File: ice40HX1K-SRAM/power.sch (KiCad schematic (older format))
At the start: 20 parts

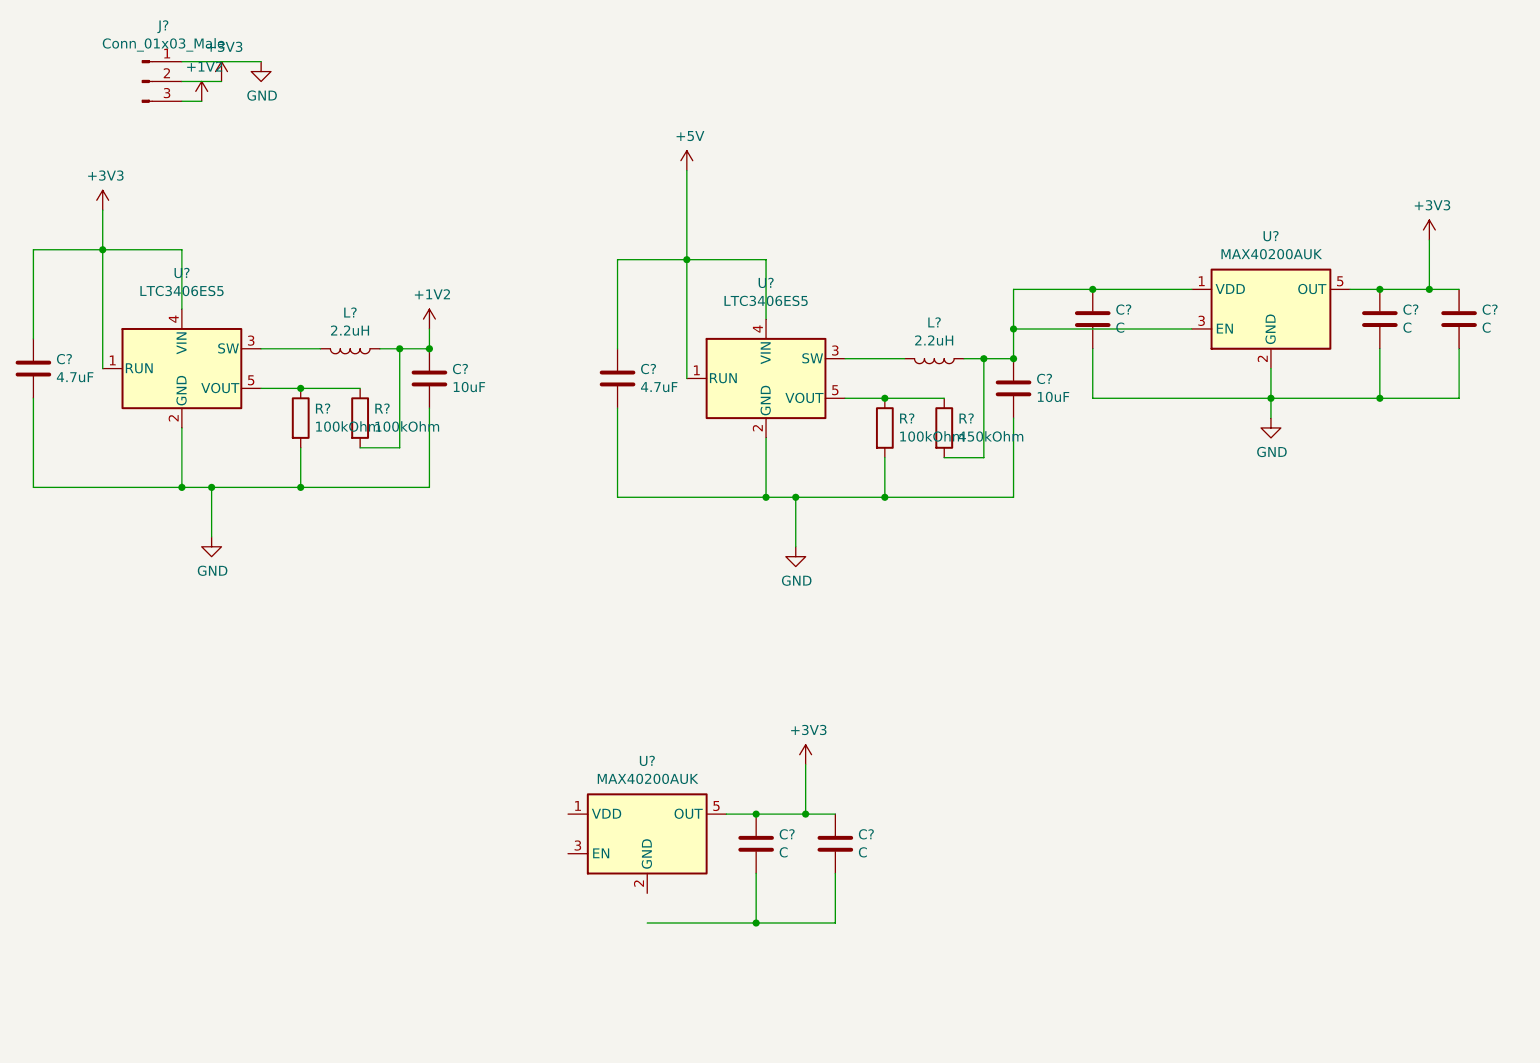
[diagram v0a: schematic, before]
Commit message: wiring FPGA nRF52 and ATSAMD11
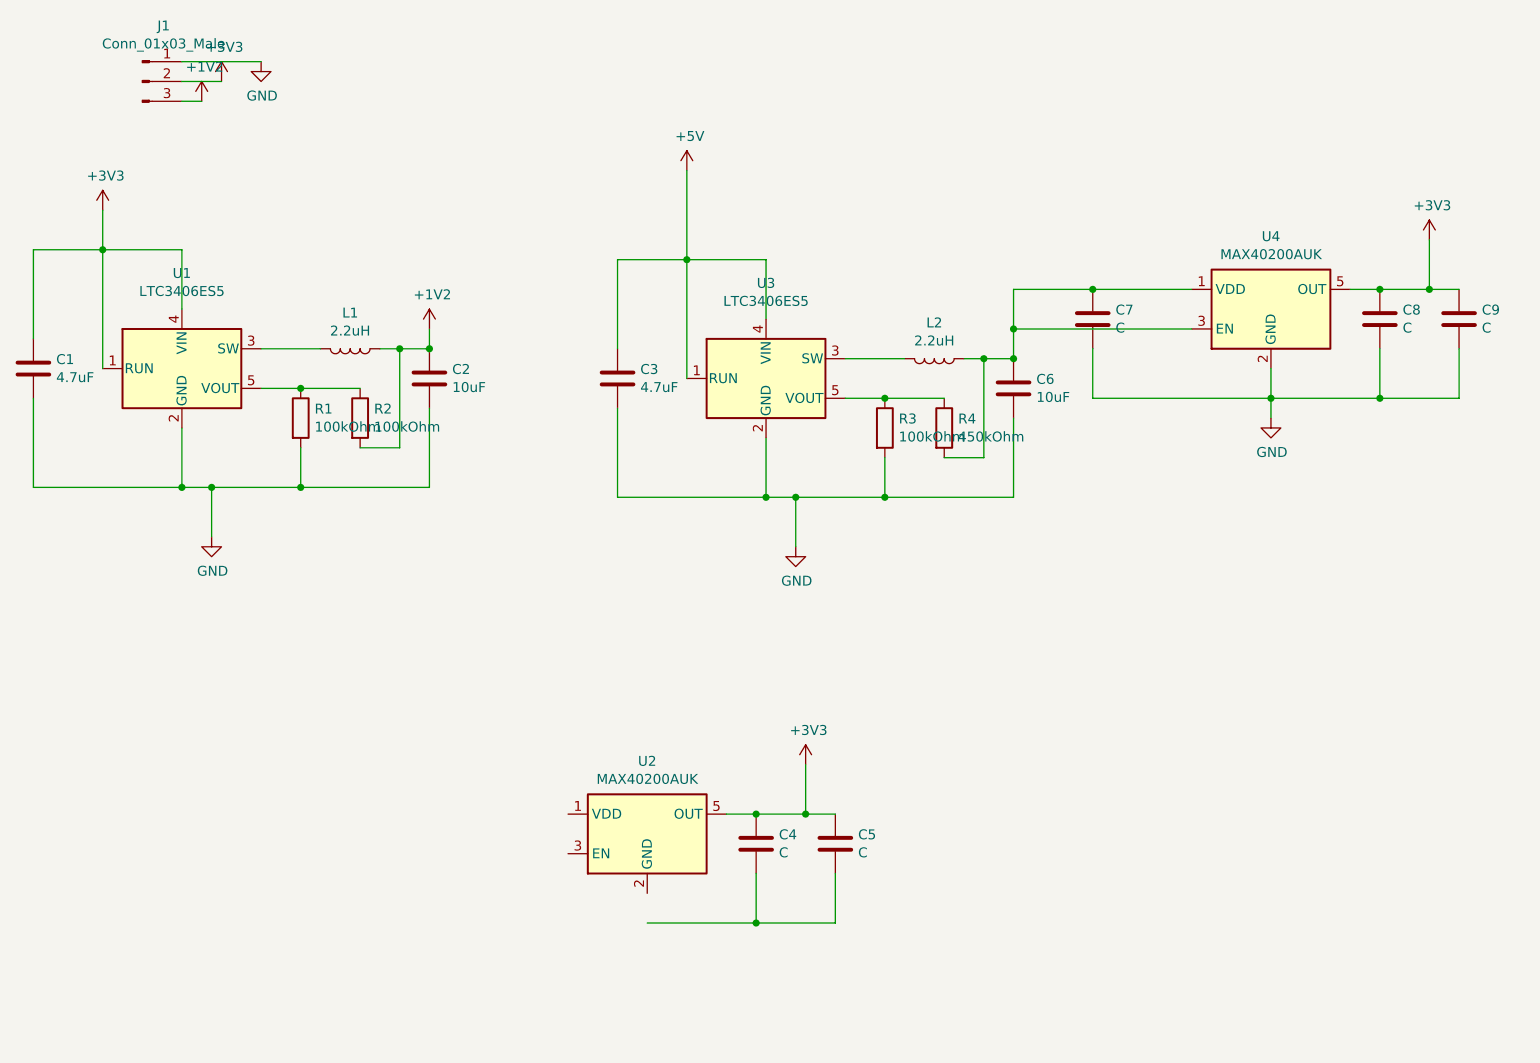
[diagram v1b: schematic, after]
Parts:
- gave numbers to parts that had none: 20
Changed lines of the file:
@@
 $EndDescr
 $Comp
-L Regulator_Switching:LTC3406ES5 U?
+L Regulator_Switching:LTC3406ES5 U1
 U 1 1 5E5E25FE
 P 1850 2500
-F 0 "U?" H 1850 2981 50  0000 C CNN
+F 0 "U1" H 1850 2981 50  0000 C CNN
 F 1 "LTC3406ES5" H 1850 2890 50  0000 C CNN
 F 2 "Package_TO_SOT_SMD:TSOT-23-5" H 2550 2250 50  0001 C CNN
@@
 $EndComp
 $Comp
-L Device:L L?
+L Device:L L1
 U 1 1 5E5E2604
 P 2700 2400
-F 0 "L?" V 2519 2400 50  0000 C CNN
+F 0 "L1" V 2519 2400 50  0000 C CNN
 F 1 "2.2uH" V 2610 2400 50  0000 C CNN
 F 2 "Inductor_SMD:L_1210_3225Metric" H 2700 2400 50  0001 C CNN
@@
 $EndComp
 $Comp
-L Device:C C?
+L Device:C C2
 U 1 1 5E5E260A
 P 3100 2550
-F 0 "C?" H 3215 2596 50  0000 L CNN
+F 0 "C2" H 3215 2596 50  0000 L CNN
 F 1 "10uF" H 3215 2505 50  0000 L CNN
 F 2 "Capacitor_SMD:C_1206_3216Metric" H 3138 2400 50  0001 C CNN
@@
 $EndComp
 $Comp
-L Device:C C?
+L Device:C C1
 U 1 1 5E5E2610
 P 1100 2500
-F 0 "C?" H 1215 2546 50  0000 L CNN
+F 0 "C1" H 1215 2546 50  0000 L CNN
 F 1 "4.7uF" H 1215 2455 50  0000 L CNN
 F 2 "Capacitor_SMD:C_1206_3216Metric" H 1138 2350 50  0001 C CNN
@@
 $EndComp
 $Comp
-L Device:R R?
+L Device:R R1
 U 1 1 5E5E2616
 P 2450 2750
-F 0 "R?" H 2520 2796 50  0000 L CNN
+F 0 "R1" H 2520 2796 50  0000 L CNN
 F 1 "100kOhm" H 2520 2705 50  0000 L CNN
 F 2 "Resistor_SMD:R_1206_3216Metric" V 2380 2750 50  0001 C CNN
@@
 $EndComp
 $Comp
-L Device:R R?
+L Device:R R2
 U 1 1 5E5E261C
 P 2750 2750
-F 0 "R?" H 2820 2796 50  0000 L CNN
+F 0 "R2" H 2820 2796 50  0000 L CNN
 F 1 "100kOhm" H 2820 2705 50  0000 L CNN
 F 2 "Resistor_SMD:R_1206_3216Metric" V 2680 2750 50  0001 C CNN
@@
 Connection ~ 2450 3100
 $Comp
-L power:+1V2 #PWR?
+L power:+1V2 #PWR06
 U 1 1 5E5E263A
 P 3100 2300
-F 0 "#PWR?" H 3100 2150 50  0001 C CNN
+F 0 "#PWR06" H 3100 2150 50  0001 C CNN
 F 1 "+1V2" H 3115 2473 50  0000 C CNN
 F 2 "" H 3100 2300 50  0001 C CNN
@@
 Connection ~ 3100 2400
 $Comp
-L power:GND #PWR?
+L power:GND #PWR03
 U 1 1 5E5E2642
 P 2000 3350
-F 0 "#PWR?" H 2000 3100 50  0001 C CNN
+F 0 "#PWR03" H 2000 3100 50  0001 C CNN
 F 1 "GND" H 2005 3177 50  0000 C CNN
 F 2 "" H 2000 3350 50  0001 C CNN
@@
 	2000 3100 2450 3100
 $Comp
-L power:+3V3 #PWR?
+L power:+3V3 #PWR01
 U 1 1 5E5E264B
 P 1450 1700
-F 0 "#PWR?" H 1450 1550 50  0001 C CNN
+F 0 "#PWR01" H 1450 1550 50  0001 C CNN
 F 1 "+3V3" H 1465 1873 50  0000 C CNN
 F 2 "" H 1450 1700 50  0001 C CNN
@@
 	1450 1700 1450 1900
 $Comp
-L Connector:Conn_01x03_Male J?
+L Connector:Conn_01x03_Male J1
 U 1 1 5E5E2652
 P 1650 1050
-F 0 "J?" H 1758 1331 50  0000 C CNN
+F 0 "J1" H 1758 1331 50  0000 C CNN
 F 1 "Conn_01x03_Male" H 1758 1240 50  0000 C CNN
 F 2 "Connector_PinHeader_2.54mm:PinHeader_1x03_P2.54mm_Vertical" H 1650 1050 50  0001 C CNN
@@
 $EndComp
 $Comp
-L power:GND #PWR?
+L power:GND #PWR05
 U 1 1 5E5E2658
 P 2250 950
-F 0 "#PWR?" H 2250 700 50  0001 C CNN
+F 0 "#PWR05" H 2250 700 50  0001 C CNN
 F 1 "GND" H 2255 777 50  0000 C CNN
 F 2 "" H 2250 950 50  0001 C CNN
@@
 $EndComp
 $Comp
-L power:+3V3 #PWR?
+L power:+3V3 #PWR04
 U 1 1 5E5E265E
 P 2050 1050
-F 0 "#PWR?" H 2050 900 50  0001 C CNN
+F 0 "#PWR04" H 2050 900 50  0001 C CNN
 F 1 "+3V3" H 2065 1223 50  0000 C CNN
 F 2 "" H 2050 1050 50  0001 C CNN
@@
 $EndComp
 $Comp
-L power:+1V2 #PWR?
+L power:+1V2 #PWR02
 U 1 1 5E5E2664
 P 1950 1150
-F 0 "#PWR?" H 1950 1000 50  0001 C CNN
+F 0 "#PWR02" H 1950 1000 50  0001 C CNN
 F 1 "+1V2" H 1965 1323 50  0000 C CNN
 F 2 "" H 1950 1150 50  0001 C CNN
@@
 	1850 950  2250 950
 $Comp
-L Regulator_Switching:LTC3406ES5 U?
+L Regulator_Switching:LTC3406ES5 U3
 U 1 1 5E5F3EED
 P 4800 2550
-F 0 "U?" H 4800 3031 50  0000 C CNN
+F 0 "U3" H 4800 3031 50  0000 C CNN
 F 1 "LTC3406ES5" H 4800 2940 50  0000 C CNN
 F 2 "Package_TO_SOT_SMD:TSOT-23-5" H 5500 2300 50  0001 C CNN
@@
 $EndComp
 $Comp
-L Device:L L?
+L Device:L L2
 U 1 1 5E5F3EF3
 P 5650 2450
-F 0 "L?" V 5469 2450 50  0000 C CNN
+F 0 "L2" V 5469 2450 50  0000 C CNN
 F 1 "2.2uH" V 5560 2450 50  0000 C CNN
 F 2 "Inductor_SMD:L_1210_3225Metric" H 5650 2450 50  0001 C CNN
@@
 $EndComp
 $Comp
-L Device:C C?
+L Device:C C6
 U 1 1 5E5F3EF9
 P 6050 2600
-F 0 "C?" H 6165 2646 50  0000 L CNN
+F 0 "C6" H 6165 2646 50  0000 L CNN
 F 1 "10uF" H 6165 2555 50  0000 L CNN
 F 2 "Capacitor_SMD:C_1206_3216Metric" H 6088 2450 50  0001 C CNN
@@
 $EndComp
 $Comp
-L Device:C C?
+L Device:C C3
 U 1 1 5E5F3EFF
 P 4050 2550
-F 0 "C?" H 4165 2596 50  0000 L CNN
+F 0 "C3" H 4165 2596 50  0000 L CNN
 F 1 "4.7uF" H 4165 2505 50  0000 L CNN
 F 2 "Capacitor_SMD:C_1206_3216Metric" H 4088 2400 50  0001 C CNN
@@
 $EndComp
 $Comp
-L Device:R R?
+L Device:R R3
 U 1 1 5E5F3F05
 P 5400 2800
-F 0 "R?" H 5470 2846 50  0000 L CNN
+F 0 "R3" H 5470 2846 50  0000 L CNN
 F 1 "100kOhm" H 5470 2755 50  0000 L CNN
 F 2 "Resistor_SMD:R_1206_3216Metric" V 5330 2800 50  0001 C CNN
@@
 $EndComp
 $Comp
-L Device:R R?
+L Device:R R4
 U 1 1 5E5F3F0B
 P 5700 2800
-F 0 "R?" H 5770 2846 50  0000 L CNN
+F 0 "R4" H 5770 2846 50  0000 L CNN
 F 1 "450kOhm" H 5770 2755 50  0000 L CNN
 F 2 "Resistor_SMD:R_0402_1005Metric" V 5630 2800 50  0001 C CNN
@@
 Connection ~ 5400 3150
 $Comp
-L power:GND #PWR?
+L power:GND #PWR08
 U 1 1 5E5F3F31
 P 4950 3400
-F 0 "#PWR?" H 4950 3150 50  0001 C CNN
+F 0 "#PWR08" H 4950 3150 50  0001 C CNN
 F 1 "GND" H 4955 3227 50  0000 C CNN
 F 2 "" H 4950 3400 50  0001 C CNN
@@
 	4950 3150 5400 3150
 $Comp
-L power:+5V #PWR?
+L power:+5V #PWR07
 U 1 1 5E5F763C
 P 4400 1500
-F 0 "#PWR?" H 4400 1350 50  0001 C CNN
+F 0 "#PWR07" H 4400 1350 50  0001 C CNN
 F 1 "+5V" H 4415 1673 50  0000 C CNN
 F 2 "" H 4400 1500 50  0001 C CNN
@@
 	4400 1500 4400 1950
 $Comp
-L Analog_Switch:MAX40200AUK U?
+L Analog_Switch:MAX40200AUK U2
 U 1 1 5E608631
 P 4200 4850
-F 0 "U?" H 4200 5217 50  0000 C CNN
+F 0 "U2" H 4200 5217 50  0000 C CNN
 F 1 "MAX40200AUK" H 4200 5126 50  0000 C CNN
 F 2 "Package_TO_SOT_SMD:SOT-23-5" H 4200 5350 50  0001 C CNN
@@
 $EndComp
 $Comp
-L Analog_Switch:MAX40200AUK U?
+L Analog_Switch:MAX40200AUK U4
 U 1 1 5E608F29
 P 7350 2200
-F 0 "U?" H 7350 2567 50  0000 C CNN
+F 0 "U4" H 7350 2567 50  0000 C CNN
 F 1 "MAX40200AUK" H 7350 2476 50  0000 C CNN
 F 2 "Package_TO_SOT_SMD:SOT-23-5" H 7350 2700 50  0001 C CNN
@@
 $EndComp
 $Comp
-L power:+3V3 #PWR?
+L power:+3V3 #PWR011
 U 1 1 5E60C10F
 P 8150 1850
-F 0 "#PWR?" H 8150 1700 50  0001 C CNN
+F 0 "#PWR011" H 8150 1700 50  0001 C CNN
 F 1 "+3V3" H 8165 2023 50  0000 C CNN
 F 2 "" H 8150 1850 50  0001 C CNN
@@
 	6050 2300 6050 2100
 $Comp
-L Device:C C?
+L Device:C C7
 U 1 1 5E60FC3E
 P 6450 2250
-F 0 "C?" H 6565 2296 50  0000 L CNN
+F 0 "C7" H 6565 2296 50  0000 L CNN
 F 1 "C" H 6565 2205 50  0000 L CNN
 F 2 "" H 6488 2100 50  0001 C CNN
@@
 	6450 2100 6950 2100
 $Comp
-L Device:C C?
+L Device:C C8
 U 1 1 5E61086D
 P 7900 2250
-F 0 "C?" H 8015 2296 50  0000 L CNN
+F 0 "C8" H 8015 2296 50  0000 L CNN
 F 1 "C" H 8015 2205 50  0000 L CNN
 F 2 "" H 7938 2100 50  0001 C CNN
@@
 $EndComp
 $Comp
-L Device:C C?
+L Device:C C9
 U 1 1 5E610C79
 P 8300 2250
-F 0 "C?" H 8415 2296 50  0000 L CNN
+F 0 "C9" H 8415 2296 50  0000 L CNN
 F 1 "C" H 8415 2205 50  0000 L CNN
 F 2 "" H 8338 2100 50  0001 C CNN
@@
 	8150 2100 8300 2100
 $Comp
-L power:GND #PWR?
+L power:GND #PWR010
 U 1 1 5E6126DE
 P 7350 2750
-F 0 "#PWR?" H 7350 2500 50  0001 C CNN
+F 0 "#PWR010" H 7350 2500 50  0001 C CNN
 F 1 "GND" H 7355 2577 50  0000 C CNN
 F 2 "" H 7350 2750 50  0001 C CNN
@@
 	7900 2650 7350 2650
 $Comp
-L power:+3V3 #PWR?
+L power:+3V3 #PWR09
 U 1 1 5E61F7B9
 P 5000 4500
-F 0 "#PWR?" H 5000 4350 50  0001 C CNN
+F 0 "#PWR09" H 5000 4350 50  0001 C CNN
 F 1 "+3V3" H 5015 4673 50  0000 C CNN
 F 2 "" H 5000 4500 50  0001 C CNN
@@
 	5000 4500 5000 4750
 $Comp
-L Device:C C?
+L Device:C C4
 U 1 1 5E61F7C0
 P 4750 4900
-F 0 "C?" H 4865 4946 50  0000 L CNN
+F 0 "C4" H 4865 4946 50  0000 L CNN
 F 1 "C" H 4865 4855 50  0000 L CNN
 F 2 "" H 4788 4750 50  0001 C CNN
@@
 $EndComp
 $Comp
-L Device:C C?
+L Device:C C5
 U 1 1 5E61F7C6
 P 5150 4900
-F 0 "C?" H 5265 4946 50  0000 L CNN
+F 0 "C5" H 5265 4946 50  0000 L CNN
 F 1 "C" H 5265 4855 50  0000 L CNN
 F 2 "" H 5188 4750 50  0001 C CNN

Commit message: wiring FPGA
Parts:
- added BT1: Battery_Cell, symbol Device:Battery_Cell
- added C?: C, symbol Device:C
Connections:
- net at U2.1 (VDD): now also U2.3 (EN), BT1.1 (+), C?.1
- net at U2.2 (GND): now also C4.2, C5.2, BT1.2 (-), C?.2
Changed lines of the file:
@@
 	4750 5050 4750 5300
 Connection ~ 4750 5300
+$Comp
+L Device:Battery_Cell BT1
+U 1 1 5E6EFF2C
+P 2950 4950
+F 0 "BT1" H 3068 5046 50  0000 L CNN
+F 1 "Battery_Cell" H 3068 4955 50  0000 L CNN
+F 2 "" V 2950 5010 50  0001 C CNN
+F 3 "~" V 2950 5010 50  0001 C CNN
+	1    2950 4950
+	1    0    0    -1
+$EndComp
 Wire Wire Line
-	4750 5300 4200 5300
+	2950 4750 3400 4750
+Wire Wire Line
+	3600 4750 3600 4950
+Wire Wire Line
+	3600 4950 3800 4950
+Connection ~ 3600 4750
+Wire Wire Line
+	3600 4750 3800 4750
+Wire Wire Line
+	2950 5050 2950 5300
+Wire Wire Line
+	2950 5300 3400 5300
+Wire Wire Line
+	4200 5150 4200 5300
+Connection ~ 4200 5300
+Wire Wire Line
+	4200 5300 4750 5300
+$Comp
+L Device:C C?
+U 1 1 5E6F85E4
+P 3400 5000
+F 0 "C?" H 3515 5046 50  0000 L CNN
+F 1 "C" H 3515 4955 50  0000 L CNN
+F 2 "" H 3438 4850 50  0001 C CNN
+F 3 "~" H 3400 5000 50  0001 C CNN
+	1    3400 5000
+	1    0    0    -1
+$EndComp
+Wire Wire Line
+	3400 4850 3400 4750
+Connection ~ 3400 4750
+Wire Wire Line
+	3400 4750 3600 4750
+Wire Wire Line
+	3400 5150 3400 5300
+Connection ~ 3400 5300
+Wire Wire Line
+	3400 5300 4200 5300
 $EndSCHEMATC

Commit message: wiring FPGA
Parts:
- C4, C7, C8: value C -> 0.1uF
- C5, C9: value C -> 10uF
- C57: renamed from C?; value C -> 0.1uF
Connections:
- net GND: now also BT1.2 (-), C4.2, C5.2, C57.2, U2.2 (GND)
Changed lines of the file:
@@
 P 6450 2250
 F 0 "C7" H 6565 2296 50  0000 L CNN
-F 1 "C" H 6565 2205 50  0000 L CNN
+F 1 "0.1uF" H 6565 2205 50  0000 L CNN
 F 2 "" H 6488 2100 50  0001 C CNN
 F 3 "~" H 6450 2250 50  0001 C CNN
@@
 P 7900 2250
 F 0 "C8" H 8015 2296 50  0000 L CNN
-F 1 "C" H 8015 2205 50  0000 L CNN
+F 1 "0.1uF" H 8015 2205 50  0000 L CNN
 F 2 "" H 7938 2100 50  0001 C CNN
 F 3 "~" H 7900 2250 50  0001 C CNN
@@
 P 8300 2250
 F 0 "C9" H 8415 2296 50  0000 L CNN
-F 1 "C" H 8415 2205 50  0000 L CNN
+F 1 "10uF" H 8415 2205 50  0000 L CNN
 F 2 "" H 8338 2100 50  0001 C CNN
 F 3 "~" H 8300 2250 50  0001 C CNN
@@
 P 4750 4900
 F 0 "C4" H 4865 4946 50  0000 L CNN
-F 1 "C" H 4865 4855 50  0000 L CNN
+F 1 "0.1uF" H 4865 4855 50  0000 L CNN
 F 2 "" H 4788 4750 50  0001 C CNN
 F 3 "~" H 4750 4900 50  0001 C CNN
@@
 P 5150 4900
 F 0 "C5" H 5265 4946 50  0000 L CNN
-F 1 "C" H 5265 4855 50  0000 L CNN
+F 1 "10uF" H 5265 4855 50  0000 L CNN
 F 2 "" H 5188 4750 50  0001 C CNN
 F 3 "~" H 5150 4900 50  0001 C CNN
@@
 	4200 5300 4750 5300
 $Comp
-L Device:C C?
+L Device:C C57
 U 1 1 5E6F85E4
 P 3400 5000
-F 0 "C?" H 3515 5046 50  0000 L CNN
-F 1 "C" H 3515 4955 50  0000 L CNN
+F 0 "C57" H 3515 5046 50  0000 L CNN
+F 1 "0.1uF" H 3515 4955 50  0000 L CNN
 F 2 "" H 3438 4850 50  0001 C CNN
 F 3 "~" H 3400 5000 50  0001 C CNN
@@
 Wire Wire Line
 	3400 5300 4200 5300
+$Comp
+L power:GND #PWR0101
+U 1 1 5E7038EC
+P 4200 5700
+F 0 "#PWR0101" H 4200 5450 50  0001 C CNN
+F 1 "GND" H 4205 5527 50  0000 C CNN
+F 2 "" H 4200 5700 50  0001 C CNN
+F 3 "" H 4200 5700 50  0001 C CNN
+	1    4200 5700
+	1    0    0    -1
+$EndComp
+Wire Wire Line
+	4200 5300 4200 5700
+$Comp
+L power:PWR_FLAG #FLG0101
+U 1 1 5E70864B
+P 2950 4750
+F 0 "#FLG0101" H 2950 4825 50  0001 C CNN
+F 1 "PWR_FLAG" H 2950 4923 50  0000 C CNN
+F 2 "" H 2950 4750 50  0001 C CNN
+F 3 "~" H 2950 4750 50  0001 C CNN
+	1    2950 4750
+	1    0    0    -1
+$EndComp
+Connection ~ 2950 4750
+$Comp
+L power:PWR_FLAG #FLG0102
+U 1 1 5E70C20E
+P 6450 2100
+F 0 "#FLG0102" H 6450 2175 50  0001 C CNN
+F 1 "PWR_FLAG" H 6450 2273 50  0000 C CNN
+F 2 "" H 6450 2100 50  0001 C CNN
+F 3 "~" H 6450 2100 50  0001 C CNN
+	1    6450 2100
+	1    0    0    -1
+$EndComp
+$Comp
+L power:PWR_FLAG #FLG0103
+U 1 1 5E70E2F6
+P 4050 1950
+F 0 "#FLG0103" H 4050 2025 50  0001 C CNN
+F 1 "PWR_FLAG" H 4050 2123 50  0000 C CNN
+F 2 "" H 4050 1950 50  0001 C CNN
+F 3 "~" H 4050 1950 50  0001 C CNN
+	1    4050 1950
+	1    0    0    -1
+$EndComp
+Connection ~ 4050 1950
 $EndSCHEMATC

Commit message: wiring FPGA
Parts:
- C1, C3: footprint Capacitor_SMD:C_1206_3216Metric -> Capacitor_SMD:C_0402_1005Metric
- C2, C6: footprint Capacitor_SMD:C_1206_3216Metric -> Capacitor_SMD:C_0603_1608Metric
- C4, C7, C8: footprint (none) -> Capacitor_SMD:C_0402_1005Metric
- C5, C9: footprint (none) -> Capacitor_SMD:C_0603_1608Metric
- R1, R2, R3: footprint Resistor_SMD:R_1206_3216Metric -> Resistor_SMD:R_0402_1005Metric
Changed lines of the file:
@@
 F 0 "C2" H 3215 2596 50  0000 L CNN
 F 1 "10uF" H 3215 2505 50  0000 L CNN
-F 2 "Capacitor_SMD:C_1206_3216Metric" H 3138 2400 50  0001 C CNN
+F 2 "Capacitor_SMD:C_0603_1608Metric" H 3138 2400 50  0001 C CNN
 F 3 "~" H 3100 2550 50  0001 C CNN
 	1    3100 2550
@@
 F 0 "C1" H 1215 2546 50  0000 L CNN
 F 1 "4.7uF" H 1215 2455 50  0000 L CNN
-F 2 "Capacitor_SMD:C_1206_3216Metric" H 1138 2350 50  0001 C CNN
+F 2 "Capacitor_SMD:C_0402_1005Metric" H 1138 2350 50  0001 C CNN
 F 3 "~" H 1100 2500 50  0001 C CNN
 	1    1100 2500
@@
 F 0 "R1" H 2520 2796 50  0000 L CNN
 F 1 "100kOhm" H 2520 2705 50  0000 L CNN
-F 2 "Resistor_SMD:R_1206_3216Metric" V 2380 2750 50  0001 C CNN
+F 2 "Resistor_SMD:R_0402_1005Metric" V 2380 2750 50  0001 C CNN
 F 3 "~" H 2450 2750 50  0001 C CNN
 	1    2450 2750
@@
 F 0 "R2" H 2820 2796 50  0000 L CNN
 F 1 "100kOhm" H 2820 2705 50  0000 L CNN
-F 2 "Resistor_SMD:R_1206_3216Metric" V 2680 2750 50  0001 C CNN
+F 2 "Resistor_SMD:R_0402_1005Metric" V 2680 2750 50  0001 C CNN
 F 3 "~" H 2750 2750 50  0001 C CNN
 	1    2750 2750
@@
 F 0 "C6" H 6165 2646 50  0000 L CNN
 F 1 "10uF" H 6165 2555 50  0000 L CNN
-F 2 "Capacitor_SMD:C_1206_3216Metric" H 6088 2450 50  0001 C CNN
+F 2 "Capacitor_SMD:C_0603_1608Metric" H 6088 2450 50  0001 C CNN
 F 3 "~" H 6050 2600 50  0001 C CNN
 	1    6050 2600
@@
 F 0 "C3" H 4165 2596 50  0000 L CNN
 F 1 "4.7uF" H 4165 2505 50  0000 L CNN
-F 2 "Capacitor_SMD:C_1206_3216Metric" H 4088 2400 50  0001 C CNN
+F 2 "Capacitor_SMD:C_0402_1005Metric" H 4088 2400 50  0001 C CNN
 F 3 "~" H 4050 2550 50  0001 C CNN
 	1    4050 2550
@@
 F 0 "R3" H 5470 2846 50  0000 L CNN
 F 1 "100kOhm" H 5470 2755 50  0000 L CNN
-F 2 "Resistor_SMD:R_1206_3216Metric" V 5330 2800 50  0001 C CNN
+F 2 "Resistor_SMD:R_0402_1005Metric" V 5330 2800 50  0001 C CNN
 F 3 "~" H 5400 2800 50  0001 C CNN
 	1    5400 2800
@@
 F 0 "C7" H 6565 2296 50  0000 L CNN
 F 1 "0.1uF" H 6565 2205 50  0000 L CNN
-F 2 "" H 6488 2100 50  0001 C CNN
+F 2 "Capacitor_SMD:C_0402_1005Metric" H 6488 2100 50  0001 C CNN
 F 3 "~" H 6450 2250 50  0001 C CNN
 	1    6450 2250
@@
 F 0 "C8" H 8015 2296 50  0000 L CNN
 F 1 "0.1uF" H 8015 2205 50  0000 L CNN
-F 2 "" H 7938 2100 50  0001 C CNN
+F 2 "Capacitor_SMD:C_0402_1005Metric" H 7938 2100 50  0001 C CNN
 F 3 "~" H 7900 2250 50  0001 C CNN
 	1    7900 2250
@@
 F 0 "C9" H 8415 2296 50  0000 L CNN
 F 1 "10uF" H 8415 2205 50  0000 L CNN
-F 2 "" H 8338 2100 50  0001 C CNN
+F 2 "Capacitor_SMD:C_0603_1608Metric" H 8338 2100 50  0001 C CNN
 F 3 "~" H 8300 2250 50  0001 C CNN
 	1    8300 2250
@@
 F 0 "C4" H 4865 4946 50  0000 L CNN
 F 1 "0.1uF" H 4865 4855 50  0000 L CNN
-F 2 "" H 4788 4750 50  0001 C CNN
+F 2 "Capacitor_SMD:C_0402_1005Metric" H 4788 4750 50  0001 C CNN
 F 3 "~" H 4750 4900 50  0001 C CNN
 	1    4750 4900
@@
 F 0 "C5" H 5265 4946 50  0000 L CNN
 F 1 "10uF" H 5265 4855 50  0000 L CNN
-F 2 "" H 5188 4750 50  0001 C CNN
+F 2 "Capacitor_SMD:C_0603_1608Metric" H 5188 4750 50  0001 C CNN
 F 3 "~" H 5150 4900 50  0001 C CNN
 	1    5150 4900
